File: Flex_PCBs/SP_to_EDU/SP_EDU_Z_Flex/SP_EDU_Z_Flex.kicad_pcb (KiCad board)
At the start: 2 copper layers, 4.5 x 64 mm, 2 parts, among them J1 Conn_01x08_Male, J2 Conn_01x08_Male

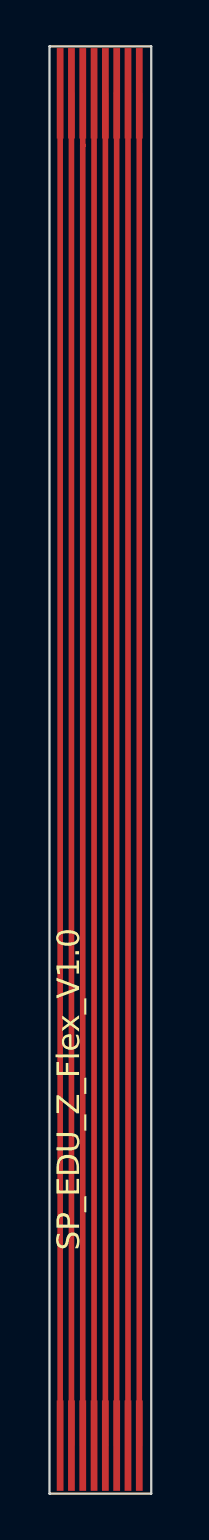
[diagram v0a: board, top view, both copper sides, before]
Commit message: replace ZF5S-*-01-T-WT and 2005280040 connectors with T1M-*-F-SH-L-FR connector
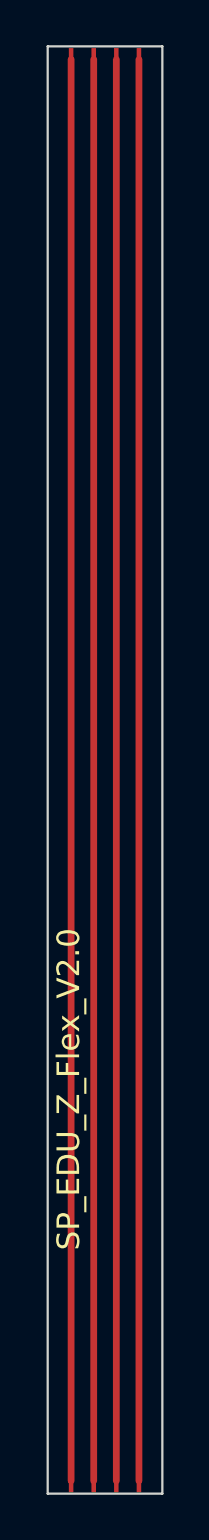
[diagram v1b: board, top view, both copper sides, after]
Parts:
- J1, J2: value Conn_01x08_Male -> Conn_01x04_Pin; footprint STS_connector:flexpcb con. -> STS_connector:flexPCB_connector_edu_sensors_new
- moved J2 5.05 mm to (123.5, 107.6), turned to 0 degrees
- moved J1 4.03 mm to (123.5, 44.8)
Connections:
- J1 pad 1: 8 -> 1
- J1 pad 2: 7 -> 2
- J1 pad 3: 6 -> 3
- J1 pad 4: 5 -> 4
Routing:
- net 8: track 59.8 -> 0.00 mm
- net 7: track 59.8 -> 0.00 mm
- net 5: track 59.8 -> 0.00 mm
- net 6: track 59.8 -> 0.00 mm
- net 4: track 59.8 -> 62.9 mm
- net 3: track 59.8 -> 62.9 mm
- net 2: track 59.8 -> 62.9 mm
- net 1: track 59.8 -> 62.9 mm
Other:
- board size 4.5 x 64 mm -> 5.1 x 64 mm
- board text added: "SP_EDU_Z_Flex_V2.0"
- board text removed: "SP_EDU_Z_Flex_V1.0"
